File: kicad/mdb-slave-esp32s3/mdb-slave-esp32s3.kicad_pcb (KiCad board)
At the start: 2 copper layers, 39 x 40 mm, 41 parts, among them J1 MDB_Connector, J2 USB_C_Receptacle_USB2.0_16P, J3 Conn_02x11_Odd_Even, SW1 SW_Push, U1 TLP785, U3 ESP32-S3FH4R2, U4 TLP785, U5 LM2594HVM-3.3, Y1 Crystal_GND24

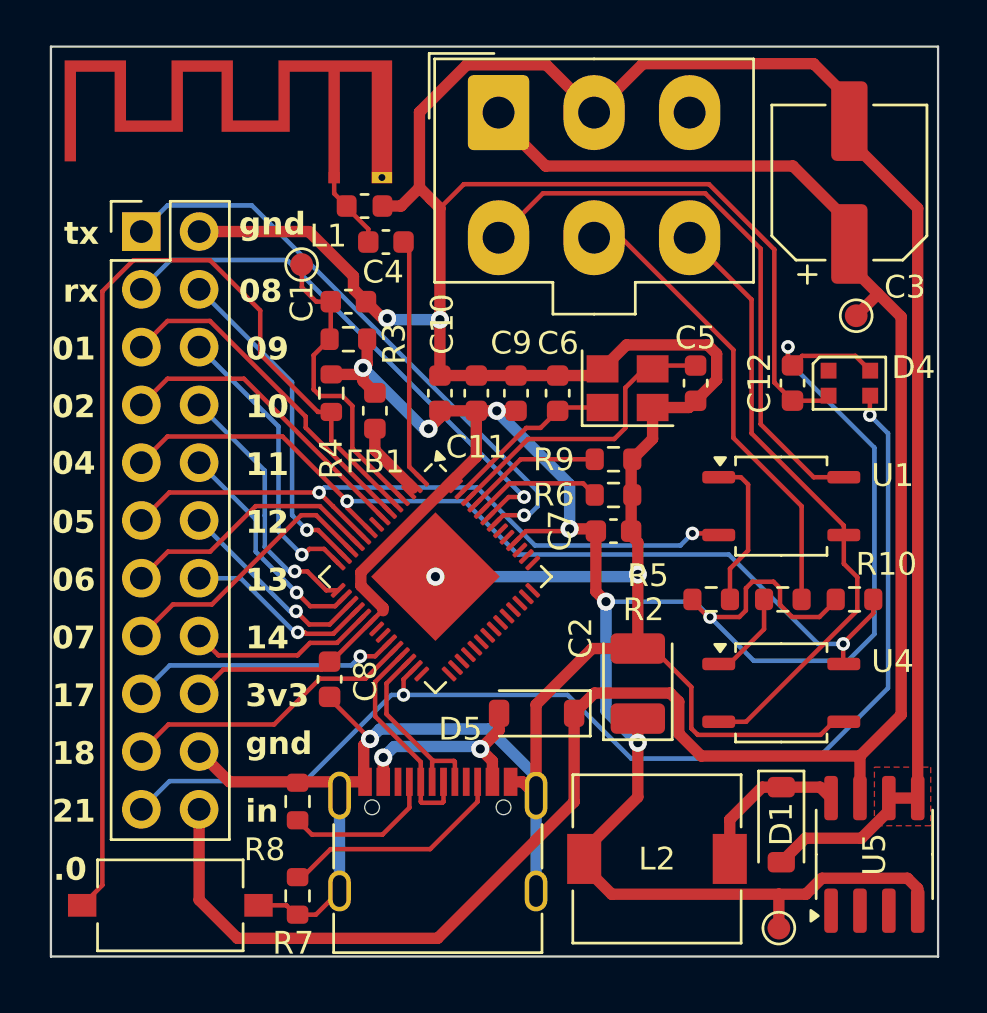
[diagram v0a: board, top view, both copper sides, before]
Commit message: Adding NTC thermal sensor
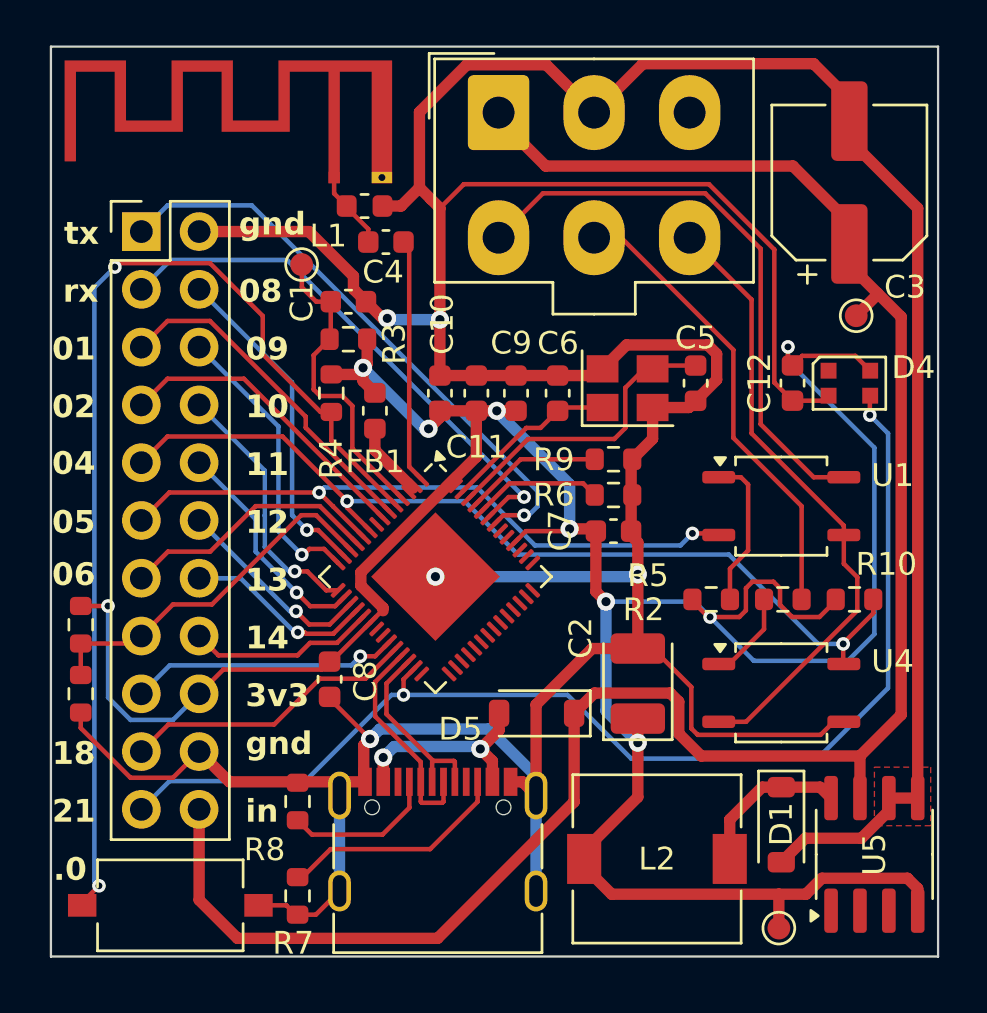
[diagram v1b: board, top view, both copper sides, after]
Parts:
- added R15: 10k, Resistor_SMD:R_0603_1608Metric, F.Cu at (169.8, 108.5)
- added TH1: Thermistor_NTC, Resistor_SMD:R_0603_1608Metric, F.Cu at (169.8, 111.5)
- moved REF** 1.63 mm to (198.9, 112.9)
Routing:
- net +3V3: track 121.3 -> 131.4 mm, vias 8 -> 9
- net GND: track 207.4 -> 214.7 mm
- net /io7: track 12.1 -> 16.2 mm
- net /boot: track 47.2 -> 47.4 mm, vias 0 -> 2

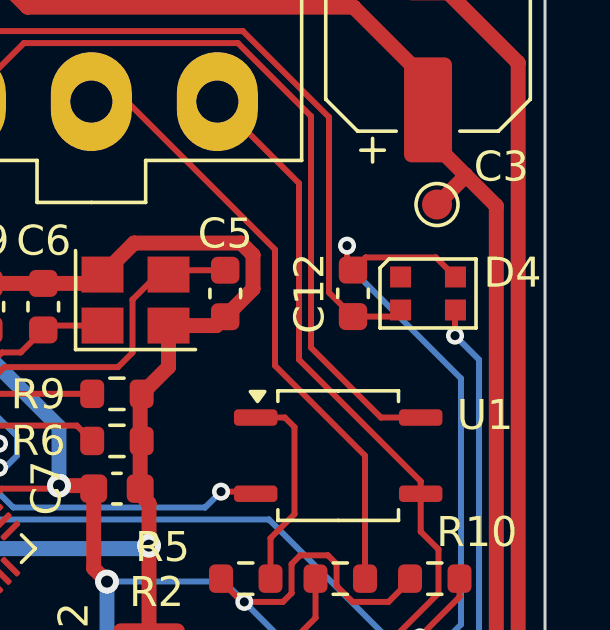
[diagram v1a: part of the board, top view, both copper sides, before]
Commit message: Updating LED footprint
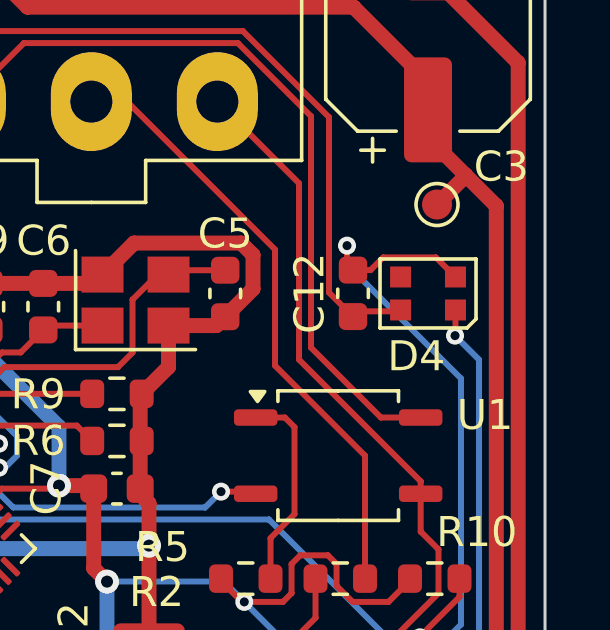
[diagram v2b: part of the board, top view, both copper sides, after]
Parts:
- moved REF** 0.34 mm to (199.0, 113.2)
- turned D4 to 180 degrees
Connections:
- D4 pad 1: unconnected-(D4-DOUT-Pad1) -> /io21
- D4 pad 2: GND -> +3V3
- D4 pad 3: /io21 -> unconnected-(D4-DOUT-Pad3)
- D4 pad 4: +3V3 -> GND

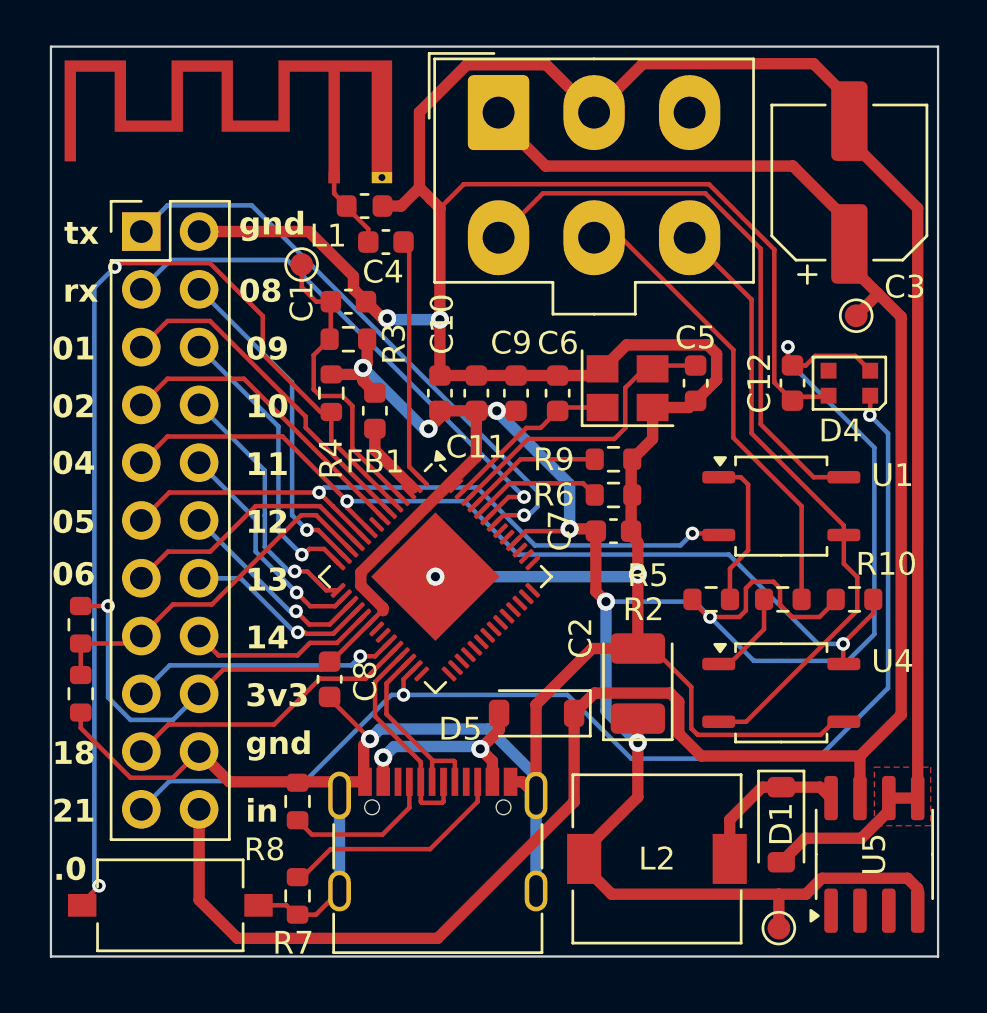
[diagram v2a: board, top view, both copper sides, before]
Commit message: mdb-slave-esp32s3 DEX level shifter routing
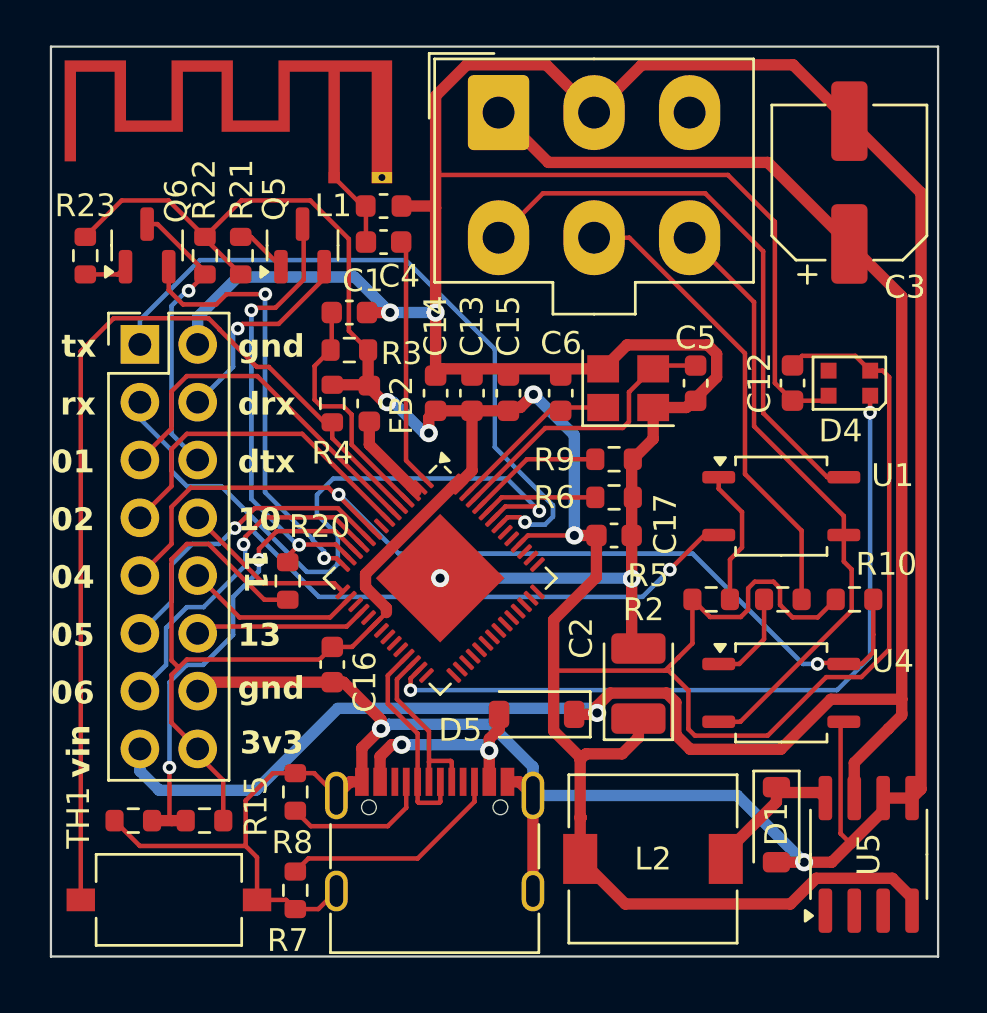
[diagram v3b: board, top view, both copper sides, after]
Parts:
- removed C10, C7, C8: 0.1uF, Capacitor_SMD:C_0603_1608Metric
- removed C11: 10uF, Capacitor_SMD:C_0603_1608Metric
- removed C9: 1uF, Capacitor_SMD:C_0603_1608Metric
- removed FB1: FerriteBead_Small, Inductor_SMD:L_0603_1608Metric
- removed J3: Conn_02x11_Odd_Even, Connector_PinHeader_2.54mm:PinHeader_2x11_P2.54mm_Vertical
- removed REF**: OSHW-Logo2_14.6x12mm_SilkScreen, Symbol:OSHW-Logo2_14.6x12mm_SilkScreen
- removed TP1, TP2, TP4: TestPoint, TestPoint:TestPoint_Pad_D1.0mm
- added C13: 10uF, Capacitor_SMD:C_0603_1608Metric, F.Cu at (187.0, 98.3)
- added C14: 0.1uF, Capacitor_SMD:C_0603_1608Metric, F.Cu at (185.4, 98.3)
- added C15: 1uF, Capacitor_SMD:C_0603_1608Metric, F.Cu at (188.6, 98.3)
- added C16: 0.1uF, Capacitor_SMD:C_0603_1608Metric, F.Cu at (180.9, 110.3)
- added C17: 0.1uF, Capacitor_SMD:C_0603_1608Metric, F.Cu at (193.3, 104.6)
- added FB2: FerriteBead_Small, Inductor_SMD:L_0603_1608Metric, F.Cu at (182.5, 98.8)
- added J7: Conn_02x08_Odd_Even, Connector_PinHeader_2.54mm:PinHeader_2x08_P2.54mm_Vertical, F.Cu at (172.4, 96.2)
- added Q5: MMBT3904, Package_TO_SOT_SMD:SOT-23, F.Cu at (179.6, 91.8)
- added Q6: MMBT3904, Package_TO_SOT_SMD:SOT-23, F.Cu at (172.7, 91.8)
- added R20: 10k, Resistor_SMD:R_0603_1608Metric, F.Cu at (178.9, 106.6)
- added R21: 4K7, Resistor_SMD:R_0603_1608Metric, F.Cu at (176.8, 92.3)
- added R22: 10k, Resistor_SMD:R_0603_1608Metric, F.Cu at (175.3, 92.3)
- added R23: 4K7, Resistor_SMD:R_0603_1608Metric, F.Cu at (170.0, 92.3)
- moved R15 10.2 mm to (175.2, 117.1), turned to 0 degrees
- moved TH1 6.04 mm to (172.1, 117.1), turned to 0 degrees
- moved L1 0.84 mm to (183.1, 90.1)
- moved C1 0.48 mm to (181.6, 94.8)
- moved R3 0.48 mm to (181.6, 96.4)
- moved R4 0.46 mm to (180.9, 98.8)
- moved R8 0.43 mm to (179.2, 115.9)
- moved R7 0.26 mm to (179.2, 120.2)
- moved U5 0.25 mm to (204.4, 118.6)
- moved SW1 0.25 mm to (173.7, 120.6)
- moved U3 0.22 mm to (185.6, 106.5)
- moved D1 0.21 mm to (200.4, 117.3)
- moved L2 0.18 mm to (195.0, 118.8)
- moved J2 0.14 mm to (185.4, 119.1)
- moved C6 0.13 mm to (190.9, 98.3)
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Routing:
- net +3V3: track 131.4 -> 169.6 mm, vias 9 -> 4
- net /io21: track 52.0 -> 33.4 mm
- net /io18: track 13.1 -> 0.00 mm
- net /dex_tx: track 0.00 -> 12.8 mm, vias 0 -> 1
- net /io17: track 11.9 -> 0.00 mm, vias 1 -> 0
- net /dex_rx: track 0.00 -> 9.20 mm, vias 0 -> 1
- net /io12: track 8.96 -> 0.00 mm, vias 1 -> 0
- net /io14: track 8.31 -> 0.00 mm
- net /io5: track 30.1 -> 37.5 mm
- net /io9: track 13.0 -> 19.4 mm, vias 1 -> 2
- net /u0rxd: track 23.7 -> 29.3 mm
- net /io8: track 14.7 -> 20.0 mm, vias 1 -> 2
- net /boot: track 47.4 -> 42.6 mm, vias 2 -> 0
- net /u0txd: track 26.0 -> 30.6 mm
- net /io7: track 16.2 -> 20.5 mm, vias 0 -> 2
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- removed copper zone on F.Cu, net GND
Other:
- board text added: "drx"
- board text added: "dtx"
- board text added: "vin"
- board text removed: ".0"
- board text removed: "07"
- board text removed: "08"
- board text removed: "09"
- board text removed: "12"
- board text removed: "14"
- board text removed: "17"
- board text removed: "18"
- board text removed: "21"
- board text removed: "in"

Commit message: Add JST Connectors for I²C and Pulse Interfaces (#46)
Added dedicated JST connectors for the I²C bus (SDA/SCL + power and GND)

Added JST connector for pulse input interface, compatible with common vending machine pulse outputs

Updated schematic symbols and PCB layout to reflect the new connectors

Routed signals following best practices for noise reduction and signal integrity
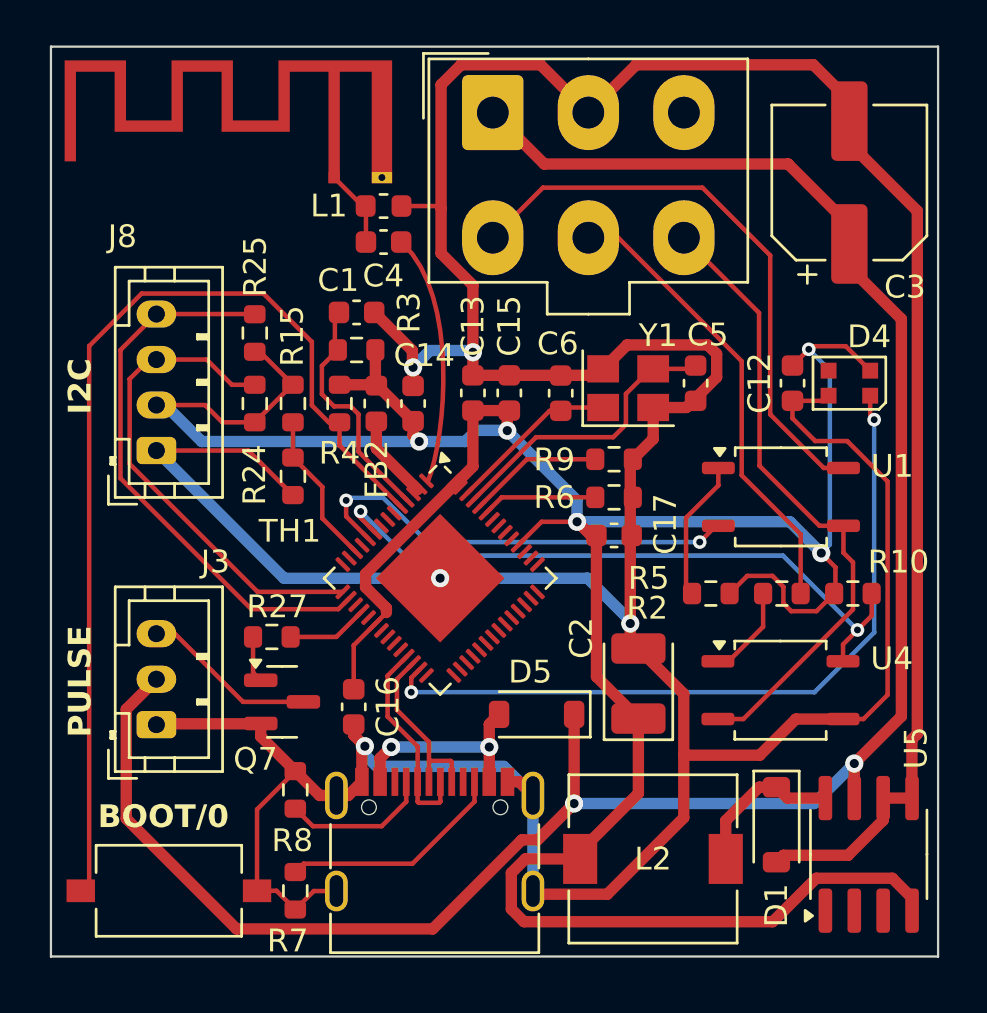
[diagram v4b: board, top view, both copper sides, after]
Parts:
- removed J7: Conn_02x08_Odd_Even, Connector_PinHeader_2.54mm:PinHeader_2x08_P2.54mm_Vertical
- removed Q5, Q6: MMBT3904, Package_TO_SOT_SMD:SOT-23
- removed R20, R22: 10k, Resistor_SMD:R_0603_1608Metric
- removed R21, R23: 4K7, Resistor_SMD:R_0603_1608Metric
- added J3: Conn_01x03_Pin, Connector_JST:JST_PH_B3B-PH-K_1x03_P2.00mm_Vertical, F.Cu at (173.1, 112.9)
- added J8: Conn_01x04_Pin, Connector_JST:JST_PH_B4B-PH-K_1x04_P2.00mm_Vertical, F.Cu at (173.1, 100.8)
- added Q7: MMBT3904, Package_TO_SOT_SMD:SOT-23, F.Cu at (178.7, 111.9)
- added R24: 4K7, Resistor_SMD:R_0603_1608Metric, F.Cu at (177.5, 98.8)
- added R25: 4K7, Resistor_SMD:R_0603_1608Metric, F.Cu at (177.5, 95.7)
- added R27: 4K7, Resistor_SMD:R_0603_1608Metric, F.Cu at (178.2, 109.0)
- added REF**: OSHW-Logo_11.4x12mm_SilkScreen, Symbol:OSHW-Logo_11.4x12mm_SilkScreen, B.Cu at (192.1, 106.8)
- moved R15 18.7 mm to (179.1, 98.8), turned to 90 degrees
- moved TH1 16.7 mm to (179.1, 102.0), turned to 90 degrees
- moved C16 2.09 mm to (181.8, 112.1)
- moved C14 1.09 mm to (184.4, 98.8)
- moved U1 0.41 mm to (200.6, 102.9)
- moved SW1 0.40 mm to (173.7, 120.2)
- moved R3 0.32 mm to (181.9, 96.4)
- moved C1 0.32 mm to (181.9, 94.8)
- moved R4 0.32 mm to (181.2, 98.8)
- moved FB2 0.31 mm to (182.8, 98.8)
- moved R10 0.27 mm to (203.8, 107.1)
- moved R2 0.26 mm to (200.6, 107.1)
- moved R5 0.26 mm to (197.5, 107.1), turned to 180 degrees
- moved J1 0.25 mm to (187.9, 86.0)
- moved U4 0.12 mm to (200.6, 111.4)
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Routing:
- net +3V3: track 169.6 -> 133.0 mm, vias 4 -> 5
- net /u0txd: track 30.6 -> 0.00 mm, vias 1 -> 0
- net /u0rxd: track 29.3 -> 0.00 mm, vias 1 -> 0
- net /io8: track 20.0 -> 0.00 mm, vias 2 -> 0
- net /io9: track 19.4 -> 0.00 mm, vias 2 -> 0
- net /io5: track 37.5 -> 19.6 mm
- net /io11: track 7.77 -> 24.8 mm
- net /io1: track 16.2 -> 0.00 mm
- net /io6: track 15.2 -> 0.00 mm, vias 1 -> 0
- net /io2: track 14.9 -> 0.00 mm
- net /io4: track 42.9 -> 28.8 mm
- net /io10: track 7.73 -> 21.7 mm
- net /io7: track 20.5 -> 6.83 mm, vias 2 -> 0
- net /dex_tx: track 12.8 -> 0.00 mm, vias 1 -> 0
- net Net-(U3-LNA_IN/RF): track 11.0 -> 0.00 mm
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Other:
- board text added: "BOOT/0"
- board text added: "I2C"
- board text added: "PULSE"
- board text removed: "01"
- board text removed: "02"
- board text removed: "04"
- board text removed: "05"
- board text removed: "06"
- board text removed: "10"
- board text removed: "11"
- board text removed: "13"
- board text removed: "3v3"
- board text removed: "drx"
- board text removed: "dtx"
- board text removed: "gnd"
- board text removed: "rx"
- board text removed: "tx"
- board text removed: "vin"

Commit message: routing..
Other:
- board text added: "3v3"
- board text added: "gnd"
- board text added: "io10"
- board text added: "io11"
- board text added: "io13"
- board text added: "vin"

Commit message: routing...
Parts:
- moved REF** 0.55 mm to (192.1, 107.3)
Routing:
- net GND: track 221.7 -> 220.8 mm
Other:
- board text added: "GND"
- board text added: "SCL"
- board text added: "SDA"
- board text added: "VIN"
- board text added: "_I2C"
- board text added: "boot/0"
- board text removed: "BOOT/0"
- board text removed: "I2C"
- board text removed: "gnd"
- board text removed: "io10"
- board text removed: "io11"
- board text removed: "io13"
- board text removed: "vin"

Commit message: routing...
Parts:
- moved REF** 1.47 mm to (193.6, 107.2)
